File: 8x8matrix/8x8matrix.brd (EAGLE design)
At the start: 60.4 x 60.5 mm, 18 parts

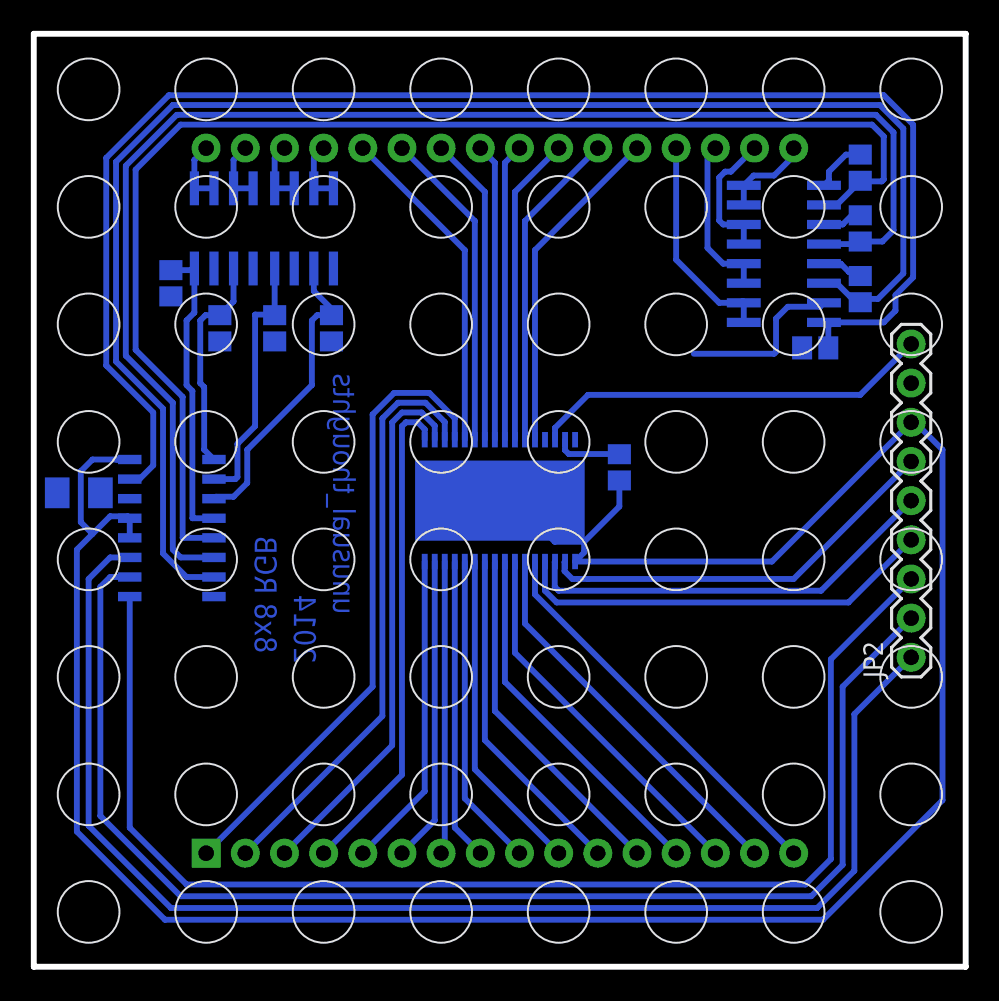
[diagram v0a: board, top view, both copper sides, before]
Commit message: cleaned up space beteween traces
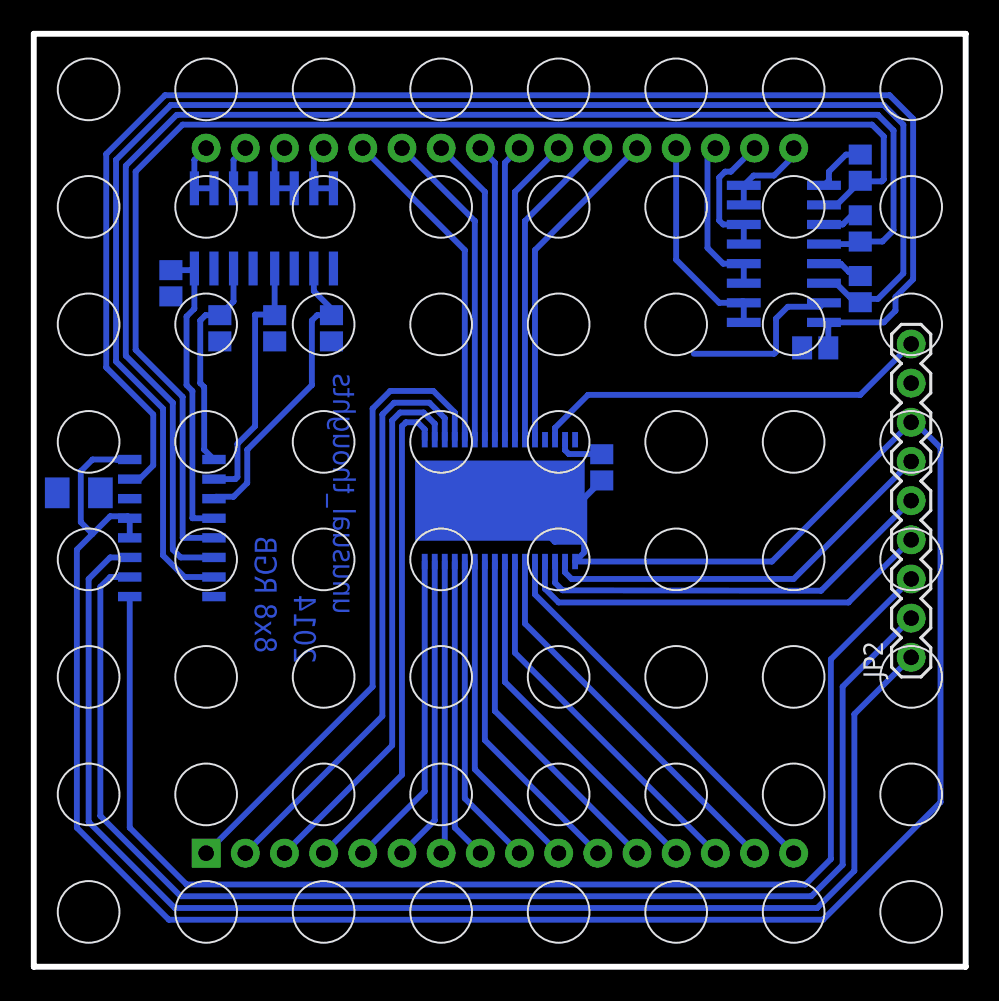
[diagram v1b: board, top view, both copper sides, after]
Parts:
- moved R1 1.14 mm to (36.8, 32.4)
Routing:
- net N$27: track 4.31 -> 3.17 mm
- net GND: track 158.5 -> 157.7 mm
- net N$16: track 40.9 -> 41.4 mm

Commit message: reprint
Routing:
- net 5.0V: track 19.8 -> 8.73 mm
- net Y1: track 92.0 -> 92.5 mm
- net Y7: track 97.5 -> 98.0 mm
- net Y2: track 84.5 -> 85.0 mm
- net Y0: track 100.0 -> 100.5 mm
